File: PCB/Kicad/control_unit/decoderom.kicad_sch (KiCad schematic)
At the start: 3 parts, among them U1 KM28C64A, U2 KM28C64A, U3 KM28C64A

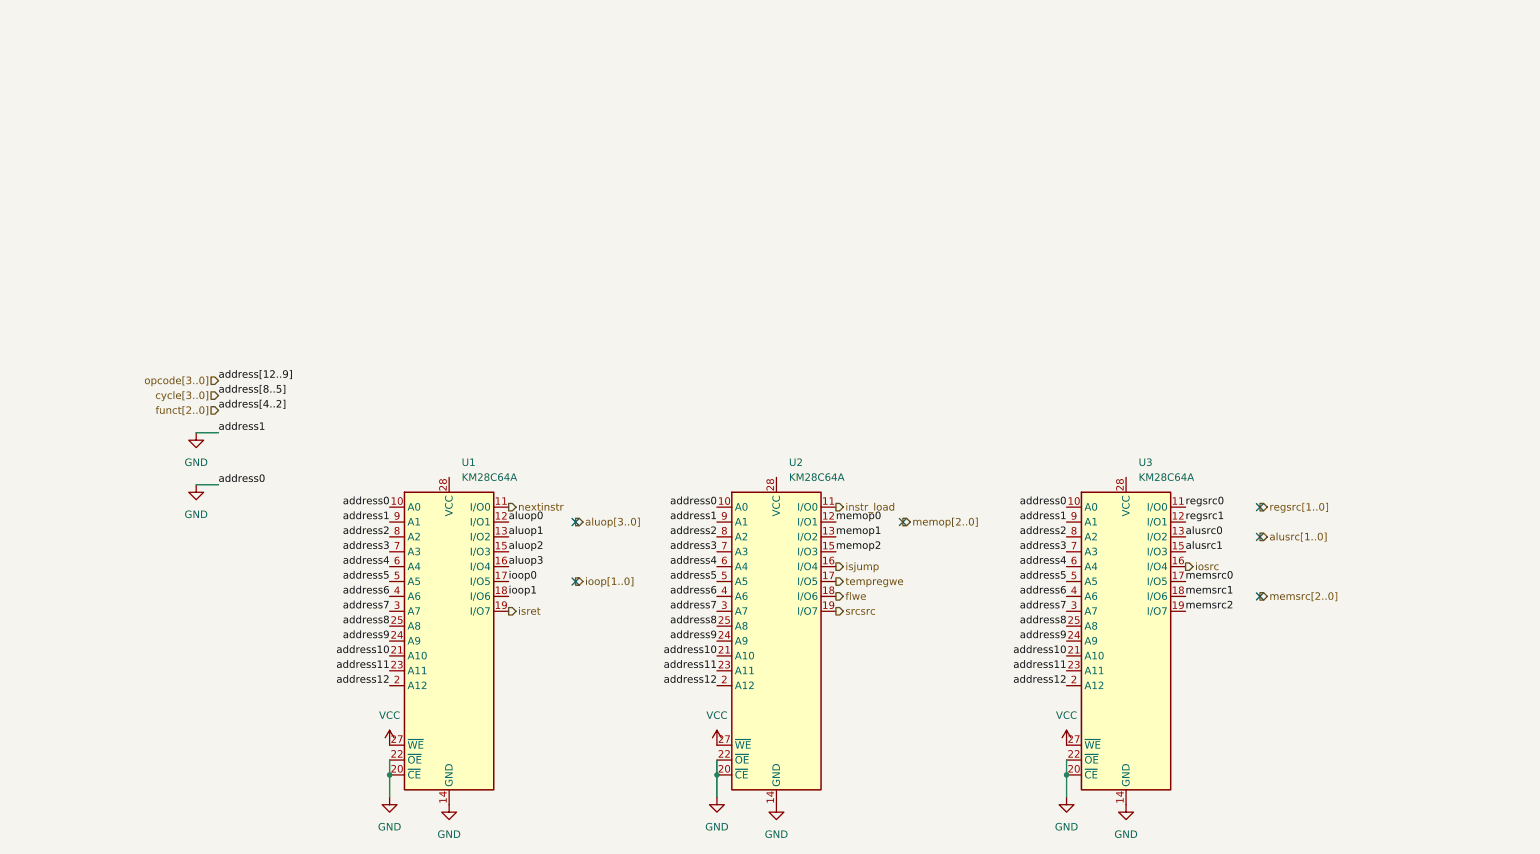
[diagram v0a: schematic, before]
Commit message: control unit schematic
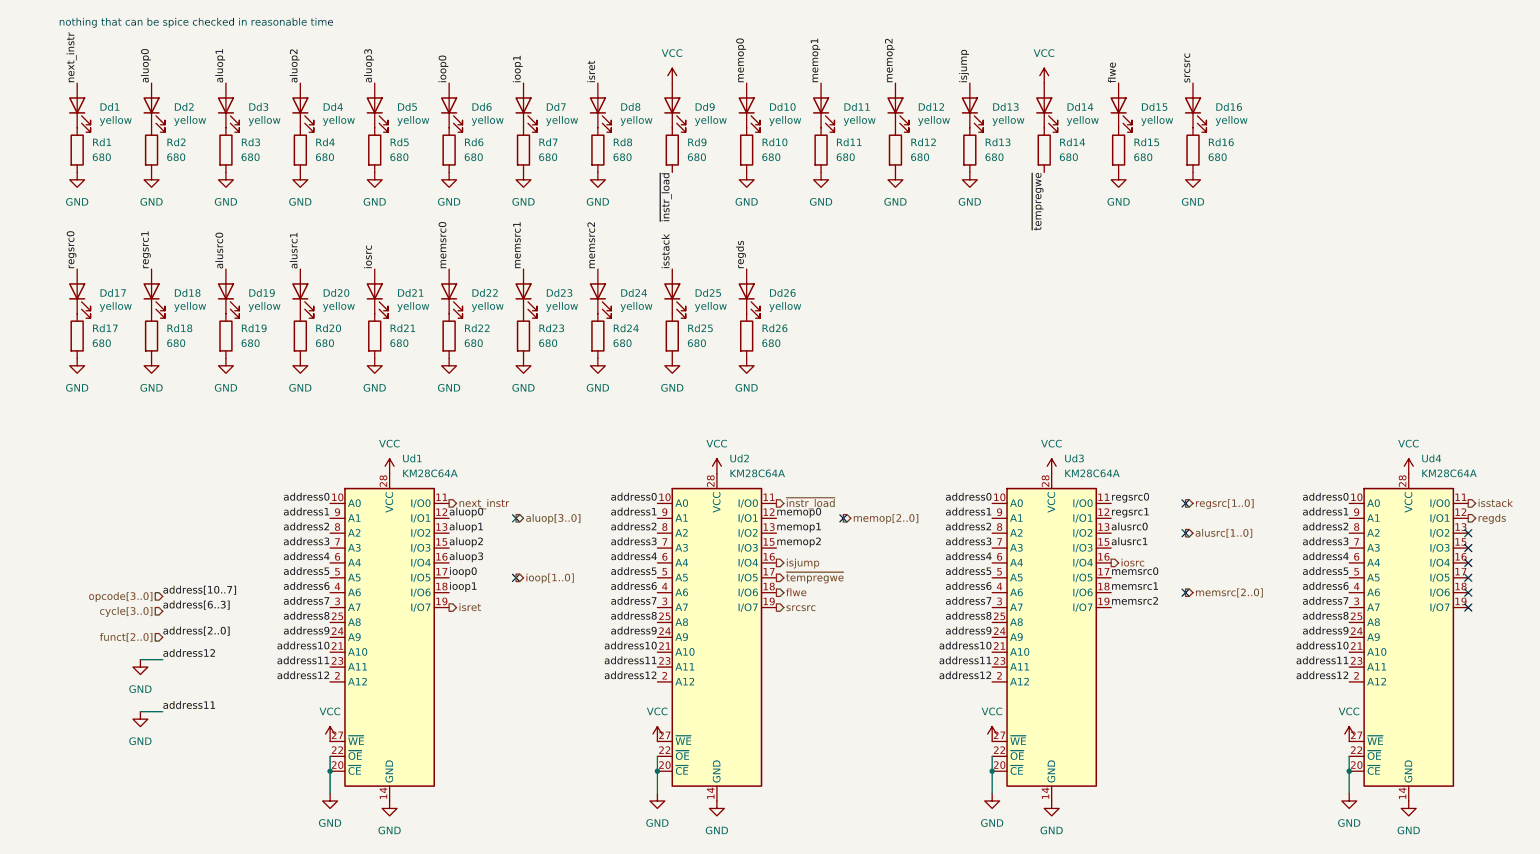
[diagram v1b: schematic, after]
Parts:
- added Dd1, Dd10, Dd11, Dd12, Dd13, Dd14, Dd15, Dd16, Dd17, Dd18, Dd19, Dd2, Dd20, Dd21, Dd22, Dd23, Dd24, Dd25, Dd26, Dd3, Dd4, Dd5, Dd6, Dd7, Dd8, Dd9: yellow, LED_SMD:LED_0603_1608Metric, symbol Device:LED
- added Rd1, Rd10, Rd11, Rd12, Rd13, Rd14, Rd15, Rd16, Rd17, Rd18, Rd19, Rd2, Rd20, Rd21, Rd22, Rd23, Rd24, Rd25, Rd26, Rd3, Rd4, Rd5, Rd6, Rd7, Rd8, Rd9: 680, Resistor_SMD:R_0402_1005Metric, symbol Device:R
- added Ud4: KM28C64A, Package_DIP:DIP-28_W15.24mm, symbol Memory_EEPROM:KM28C64A
- renumbered U1 to Ud1, U2 to Ud2, U3 to Ud3
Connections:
- net address11 is gone; now on net GND: Ud1.23 (A11), Ud2.23 (A11), Ud3.23 (A11)
- net address12 is gone; now on net GND: Ud1.2 (A12), Ud2.2 (A12), Ud3.2 (A12)
- net GND: now also Rd1.2, Rd10.2, Rd11.2, Rd12.2, Rd13.2, Rd15.2, Rd16.2, Rd17.2, Rd18.2, Rd19.2, Rd2.2, Rd20.2, Rd21.2, Rd22.2, Rd23.2, Rd24.2, Rd25.2, Rd26.2, Rd3.2, Rd4.2, Rd5.2, Rd6.2, Rd7.2, Rd8.2, Ud4.14 (GND), Ud4.2 (A12), Ud4.20 (~{CE}), Ud4.22 (~{OE}), Ud4.23 (A11); no longer Ud1.10 (A0), Ud1.9 (A1), Ud2.10 (A0), Ud2.9 (A1), Ud3.10 (A0), Ud3.9 (A1)
- net VCC: now also Ud1.28 (VCC), Ud2.28 (VCC), Ud3.28 (VCC), Dd14.2 (A), Dd9.2 (A), Ud4.27 (~{WE}), Ud4.28 (VCC)
- net address10: now also Ud4.21 (A10)
- net address2: now also Ud4.8 (A2)
- net address3: now also Ud4.7 (A3)
- net address4: now also Ud4.6 (A4)
- net address5: now also Ud4.5 (A5)
- net address6: now also Ud4.4 (A6)
- net address7: now also Ud4.3 (A7)
- net address8: now also Ud4.25 (A8)
- net address9: now also Ud4.24 (A9)
- net aluop0: now also Dd2.2 (A)
- net aluop1: now also Dd3.2 (A)
- net aluop2: now also Dd4.2 (A)
- net aluop3: now also Dd5.2 (A)
- net alusrc0: now also Dd19.2 (A)
- net alusrc1: now also Dd20.2 (A)
- net flwe: now also Dd15.2 (A)
- net ioop0: now also Dd6.2 (A)
- net ioop1: now also Dd7.2 (A)
- net iosrc: now also Dd21.2 (A)
- net isjump: now also Dd13.2 (A)
- net isret: now also Dd8.2 (A)
- net memop0: now also Dd10.2 (A)
- net memop1: now also Dd11.2 (A)
- net memop2: now also Dd12.2 (A)
- net memsrc0: now also Dd22.2 (A)
- net memsrc1: now also Dd23.2 (A)
- net memsrc2: now also Dd24.2 (A)
- net regsrc0: now also Dd17.2 (A)
- net regsrc1: now also Dd18.2 (A)
- net srcsrc: now also Dd16.2 (A)
- net instr_load renamed ~{instr_load}
- net ~{instr_load}: now also Rd9.2
- net nextinstr renamed next_instr
- net next_instr: now also Dd1.2 (A)
- net tempregwe renamed ~{tempregwe}
- net ~{tempregwe}: now also Rd14.2
- new net: Dd19.1 (K), Rd19.1
- new net: Dd14.1 (K), Rd14.1
- new net: Dd4.1 (K), Rd4.1
- new net: Dd3.1 (K), Rd3.1
- new net: Dd23.1 (K), Rd23.1
- new net: Dd25.1 (K), Rd25.1
- new net: Dd20.1 (K), Rd20.1
- new net: Dd11.1 (K), Rd11.1
- new net: Dd1.1 (K), Rd1.1
- new net: Dd6.1 (K), Rd6.1
- new net: Dd10.1 (K), Rd10.1
- new net: Dd17.1 (K), Rd17.1
- new net: Dd24.1 (K), Rd24.1
- new net: Dd12.1 (K), Rd12.1
- new net: Dd5.1 (K), Rd5.1
- new net: Dd22.1 (K), Rd22.1
- new net: Dd7.1 (K), Rd7.1
- new net: Dd16.1 (K), Rd16.1
- new net: Dd9.1 (K), Rd9.1
- new net: Dd26.1 (K), Rd26.1
- new net: Dd2.1 (K), Rd2.1
- new net: Dd8.1 (K), Rd8.1
- new net: Dd13.1 (K), Rd13.1
- new net: Dd21.1 (K), Rd21.1
- new net: Dd15.1 (K), Rd15.1
- new net: Dd18.1 (K), Rd18.1
- new net address0: Ud1.10 (A0), Ud2.10 (A0), Ud3.10 (A0), Ud4.10 (A0)
- new net address1: Ud1.9 (A1), Ud2.9 (A1), Ud3.9 (A1), Ud4.9 (A1)
- new net isstack: Dd25.2 (A), Ud4.11 (I/O0)
- new net regds: Dd26.2 (A), Ud4.12 (I/O1)
- no-connect marks 6 -> 12
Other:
- note added: "nothing that can be spice checked in reasonable time"
- company: (none) -> AGH Logic Unit
- title: (none) -> Decoder
- moved on the sheet: Ud1, Ud2, Ud3
